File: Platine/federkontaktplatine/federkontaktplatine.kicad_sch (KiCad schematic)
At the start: 15 parts, among them J1 Conn_01x07

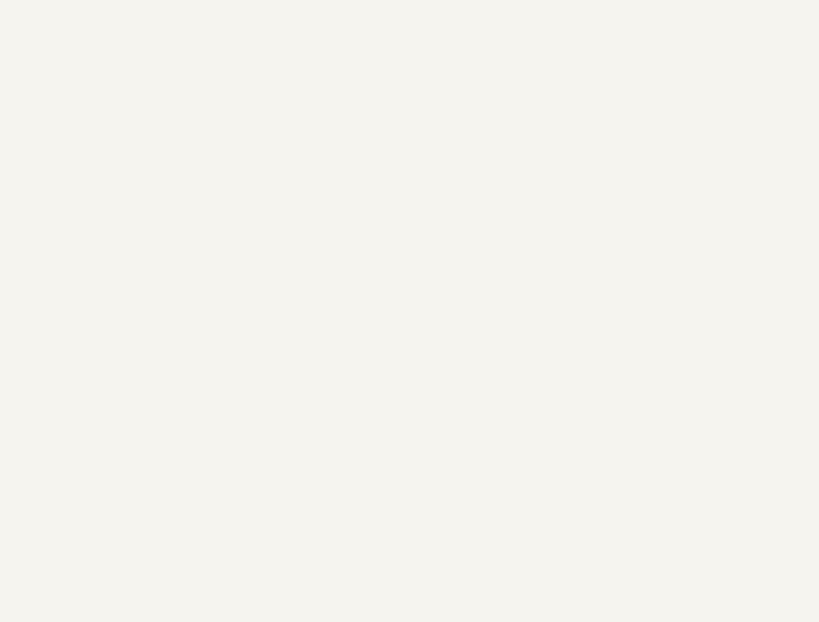
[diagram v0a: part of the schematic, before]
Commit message: montagepunkte untere platine
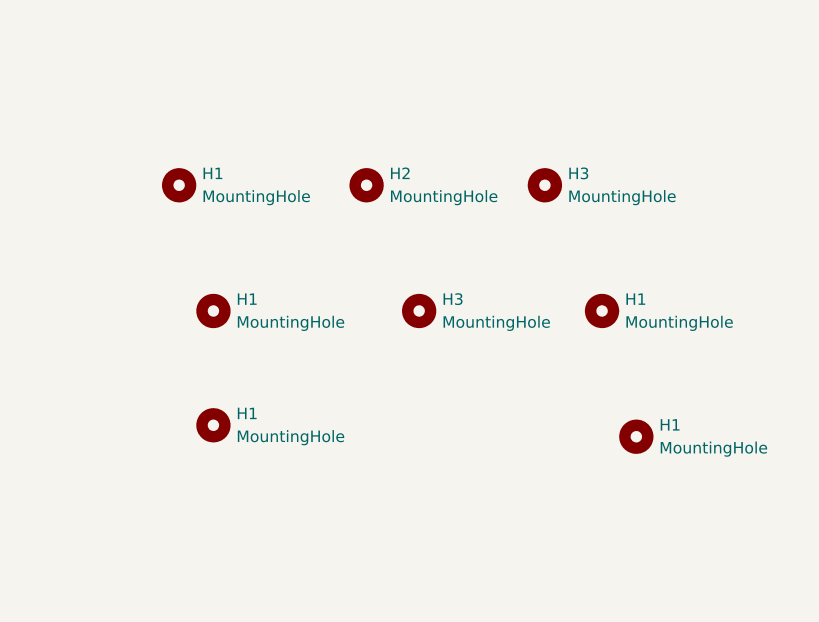
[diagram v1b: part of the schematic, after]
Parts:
- added H1 (x5), H2, H3 (x2): MountingHole, MountingHole:MountingHole_3.2mm_M3_DIN965, symbol Mechanical:MountingHole

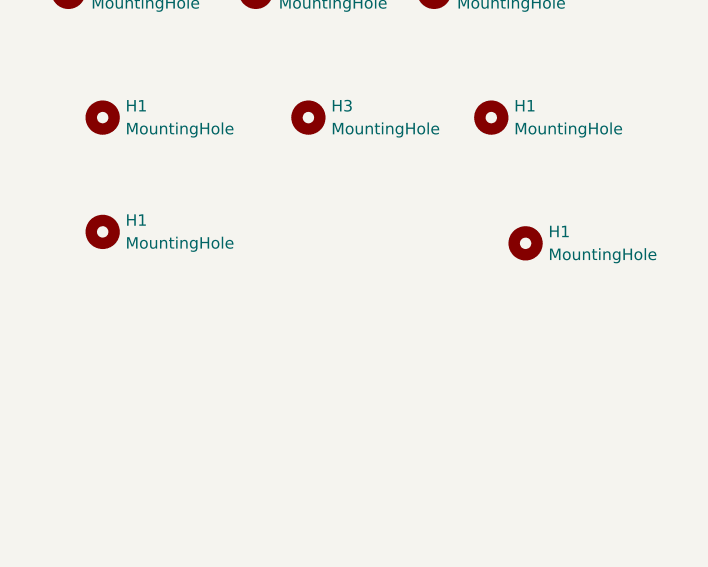
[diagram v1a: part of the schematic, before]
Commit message: montagelöcher untere platte
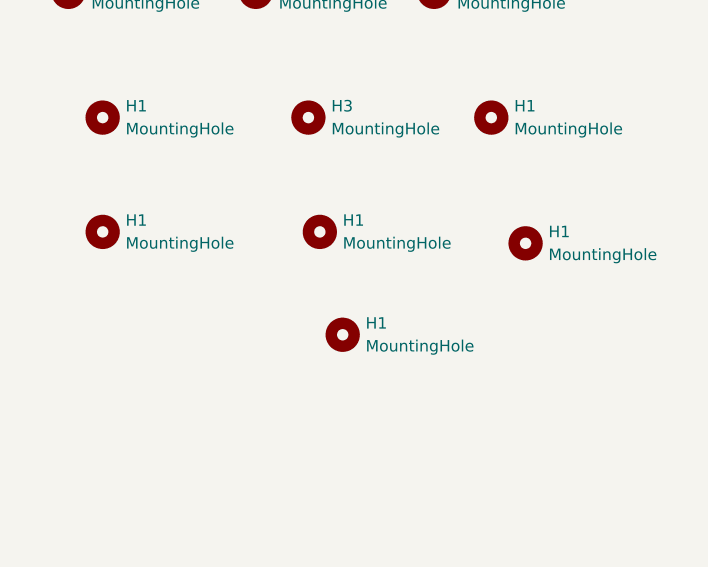
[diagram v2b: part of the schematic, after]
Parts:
- added H1 (x2): MountingHole, MountingHole:MountingHole_3.2mm_M3_DIN965, symbol Mechanical:MountingHole
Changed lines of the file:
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@@
+    )
+  )
+  (symbol (lib_id "Mechanical:MountingHole") (at 222.25 140.97 0) (unit 1)
+    (in_bom yes) (on_board yes) (dnp no) (fields_autoplaced)
+    (property "Reference" "H1" (at 224.79 139.6999 0)
+      (effects (font (size 1.27 1.27)) (justify left))
+    )
+    (property "Value" "MountingHole" (at 224.79 142.2399 0)
+      (effects (font (size 1.27 1.27)) (justify left))
+    )
+    (property "Footprint" "MountingHole:MountingHole_3.2mm_M3_DIN965" (at 222.25 140.97 0)
+      (effects (font (size 1.27 1.27)) hide)
+    )
+    (property "Datasheet" "~" (at 222.25 140.97 0)
+      (effects (font (size 1.27 1.27)) hide)
+    )
+    (instances
+      (project "FTCMS_V2.2"
+        (path "/30da9297-09e7-47e7-9d66-9d536b8d0426"
+          (reference "H1") (unit 1)
+        )
+      )
+      (project "federkontaktplatine"
+        (path "/67804148-9fb2-45a4-a226-f3c6005bfe46"
+          (reference "H2") (unit 1)
+        )
+      )
+      (project "FTCMS_PCB_v2.2"
+        (path "/83a6a285-13b6-4ec8-ae72-c2fe713cc487"
+          (reference "H1") (unit 1)
+        )
+      )
     )
   )
@@
         )
       )
+    )
+  )
+  (symbol (lib_id "Mechanical:MountingHole") (at 219.71 129.54 0) (unit 1)
+    (in_bom yes) (on_board yes) (dnp no) (fields_autoplaced)
+    (property "Reference" "H1" (at 222.25 128.2699 0)
+      (effects (font (size 1.27 1.27)) (justify left))
+    )
+    (property "Value" "MountingHole" (at 222.25 130.8099 0)
+      (effects (font (size 1.27 1.27)) (justify left))
+    )
+    (property "Footprint" "MountingHole:MountingHole_3.2mm_M3_DIN965" (at 219.71 129.54 0)
+      (effects (font (size 1.27 1.27)) hide)
+    )
+    (property "Datasheet" "~" (at 219.71 129.54 0)
+      (effects (font (size 1.27 1.27)) hide)
+    )
+    (instances
+      (project "FTCMS_V2.2"
+        (path "/30da9297-09e7-47e7-9d66-9d536b8d0426"
+          (reference "H1") (unit 1)
+        )
+      )
+      (project "federkontaktplatine"
+        (path "/67804148-9fb2-45a4-a226-f3c6005bfe46"
+          (reference "H1") (unit 1)
+        )
+      )
+      (project "FTCMS_PCB_v2.2"
+        (path "/83a6a285-13b6-4ec8-ae72-c2fe713cc487"
+          (reference "H1") (unit 1)
+        )
+      )
